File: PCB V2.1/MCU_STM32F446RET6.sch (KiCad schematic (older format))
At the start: 39 parts, among them J1 20021121-00010C4LF, J2 0475890001-MicroUSBPort, P2 CONN_01X03, SW1 B3U-1000P, U1 STM32F446RET6_-_TQFP64, X1 ABM3B8.000MHZB2T, X2 ABS07-32.768KHZ-9-T

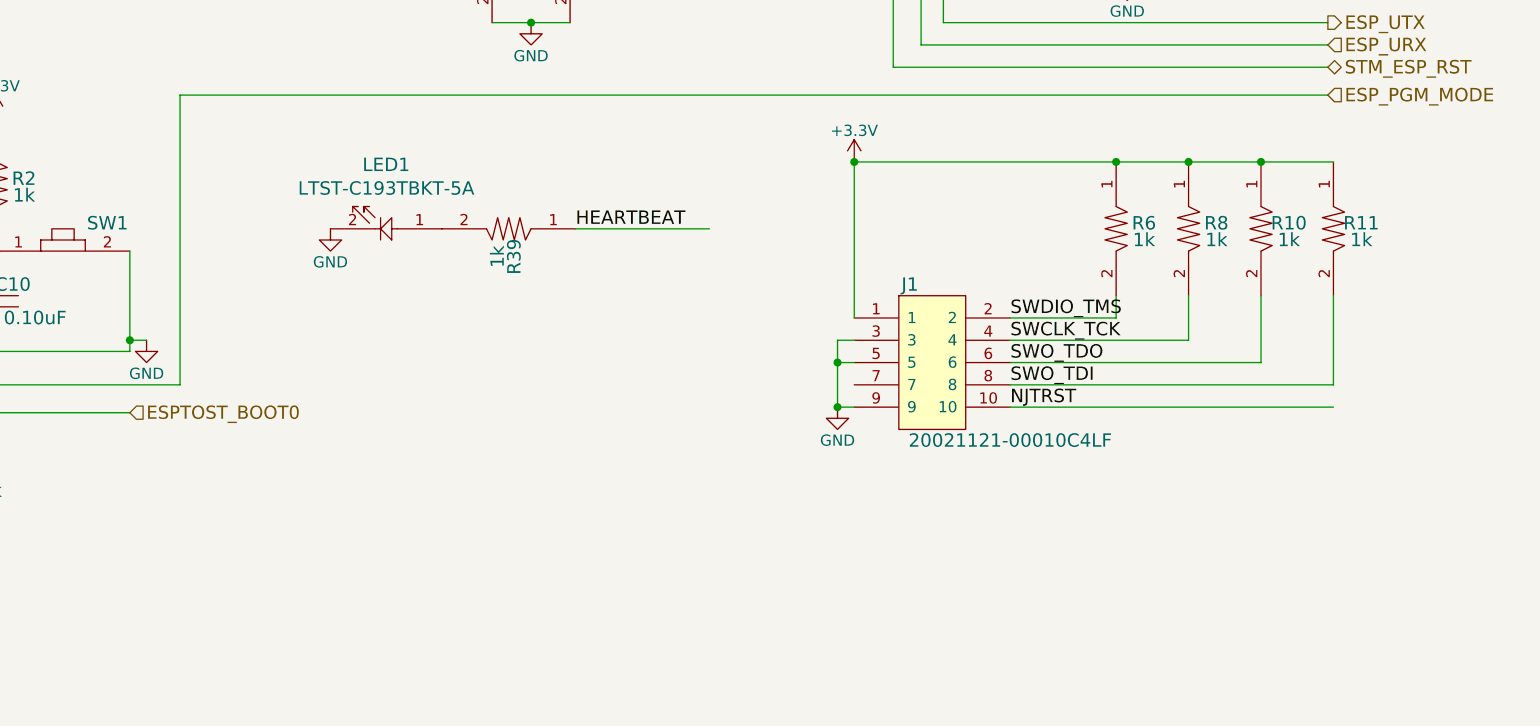
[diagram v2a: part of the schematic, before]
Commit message: DRC clear
all design rule violations cleared.
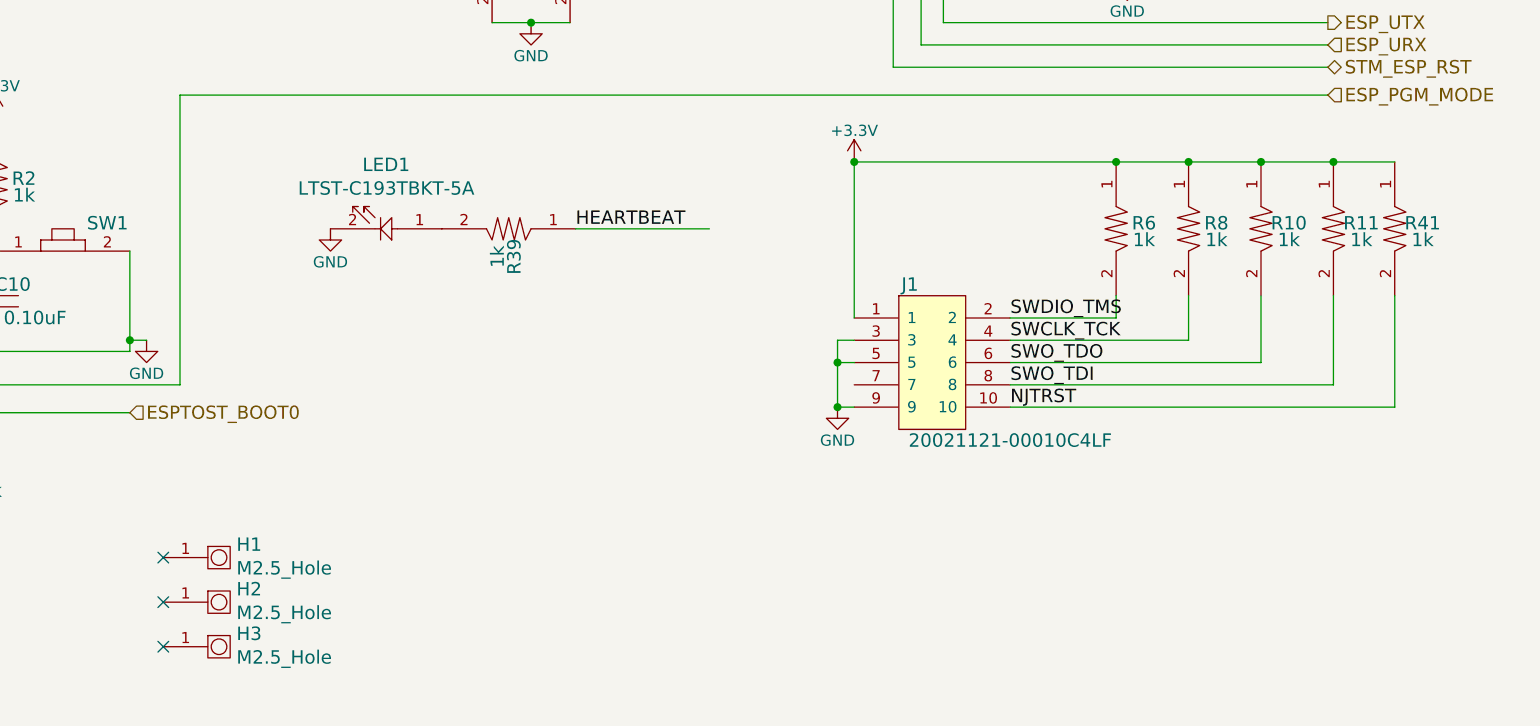
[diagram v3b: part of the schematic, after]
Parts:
- added H1, H2, H3: M2.5_Hole, PCB_Footprints:M2.5_HOLE, symbol M2.5_Hole
- added R41: RC1005F102CS, PCB_Footprints:R0402, symbol RC1005F102CS
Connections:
- wire segments 129 -> 130
- no-connect marks 0 -> 3
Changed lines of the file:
@@
 	10450 6075 10450 5675
 Wire Wire Line
-	9000 6175 10450 6175
-Wire Wire Line
-	8300 5075 10450 5075
+	9000 6175 10725 6175
+Wire Wire Line
+	8300 5075 10725 5075
 Wire Wire Line
 	8300 5075 8300 5775
@@
 	8900 1375 8900 1650
 Connection ~ 8900 1650
+$Comp
+L RC1005F102CS R41
+U 1 1 57E8DE5F
+P 10725 5375
+F 0 "R41" V 10700 5500 60  0000 C CNN
+F 1 "RC1005F102CS" H 10725 5225 60  0001 C CNN
+F 2 "PCB_Footprints:R0402" H 10325 5625 60  0001 C CNN
+F 3 "https://media.digikey.com/pdf/Data%20Sheets/Samsung%20PDFs/RC_Series_ds.pdf" H 10425 5825 60  0001 C CNN
+F 4 "0.00173 @ 5000" H 12275 7325 60  0001 C CNN "Cost"
+F 5 "5 Sept 2016" H 10625 5925 60  0001 C CNN "Date Created"
+F 6 "5 Sept 2016" H 10725 6025 60  0001 C CNN "Date Modified"
+F 7 "Adam Vadala-Roth" H 10825 6125 60  0001 C CNN "Designer"
+F 8 "0.4mm" H 10925 6225 60  0001 C CNN "Height"
+F 9 "Yes" H 11025 6325 60  0001 C CNN "RHoS?"
+F 10 "Samsung Electro-Mechanics America, Inc." H 11125 6425 60  0001 C CNN "MFR"
+F 11 "RC1005F102CS" H 11225 6525 60  0001 C CNN "MFR#"
+F 12 "SMT/SMD" H 11325 6625 60  0001 C CNN "Mounting"
+F 13 "2" H 11425 6725 60  0001 C CNN "Pin Count#"
+F 14 "Active" H 11525 6825 60  0001 C CNN "Status"
+F 15 "%" H 11625 6925 60  0001 C CNN "Tolerance"
+F 16 "passive" H 11725 7025 60  0001 C CNN "Type"
+F 17 "N/A" H 11825 7125 60  0001 C CNN "Voltage"
+F 18 "1/16" H 11925 7225 60  0001 C CNN "Wattage"
+F 19 "1k" V 10775 5500 60  0000 C CNN "Component-Value"
+F 20 "RES SMD 1K OHM 1% 1/16W 0402" H 12125 7425 60  0001 C CNN "Description"
+	1    10725 5375
+	0    1    1    0
+$EndComp
+Connection ~ 10450 5075
+Wire Wire Line
+	10725 6175 10725 5675
+$Comp
+L M2.5_Hole H1
+U 1 1 57E90C74
+P 5450 6850
+F 0 "H1" H 5528 6908 60  0000 L CNN
+F 1 "M2.5_Hole" H 5528 6802 60  0000 L CNN
+F 2 "PCB_Footprints:M2.5_HOLE" H 5075 7300 197 0001 C CNN
+F 3 "" H 5450 6850 197 0001 C CNN
+	1    5450 6850
+	1    0    0    -1
+$EndComp
+$Comp
+L M2.5_Hole H2
+U 1 1 57E90E9E
+P 5450 7050
+F 0 "H2" H 5528 7108 60  0000 L CNN
+F 1 "M2.5_Hole" H 5528 7002 60  0000 L CNN
+F 2 "PCB_Footprints:M2.5_HOLE" H 5075 7500 197 0001 C CNN
+F 3 "" H 5450 7050 197 0001 C CNN
+	1    5450 7050
+	1    0    0    -1
+$EndComp
+$Comp
+L M2.5_Hole H3
+U 1 1 57E90F41
+P 5450 7250
+F 0 "H3" H 5528 7308 60  0000 L CNN
+F 1 "M2.5_Hole" H 5528 7202 60  0000 L CNN
+F 2 "PCB_Footprints:M2.5_HOLE" H 5075 7700 197 0001 C CNN
+F 3 "" H 5450 7250 197 0001 C CNN
+	1    5450 7250
+	1    0    0    -1
+$EndComp
+NoConn ~ 5200 6850
+NoConn ~ 5200 7050
+NoConn ~ 5200 7250
 $EndSCHEMATC

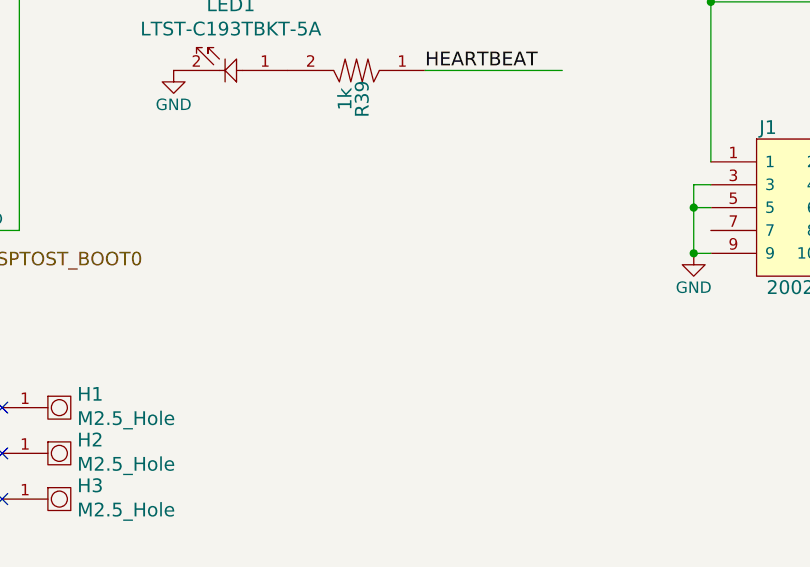
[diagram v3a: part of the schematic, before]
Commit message: 3D and Tweaks
3D files added for components for proper 3D rneder of the board. Board
tweaked, additional ground pours and sticking under neath the ESP-09,
cleaned up routign of JTAG , added labeling of all the pin signals.
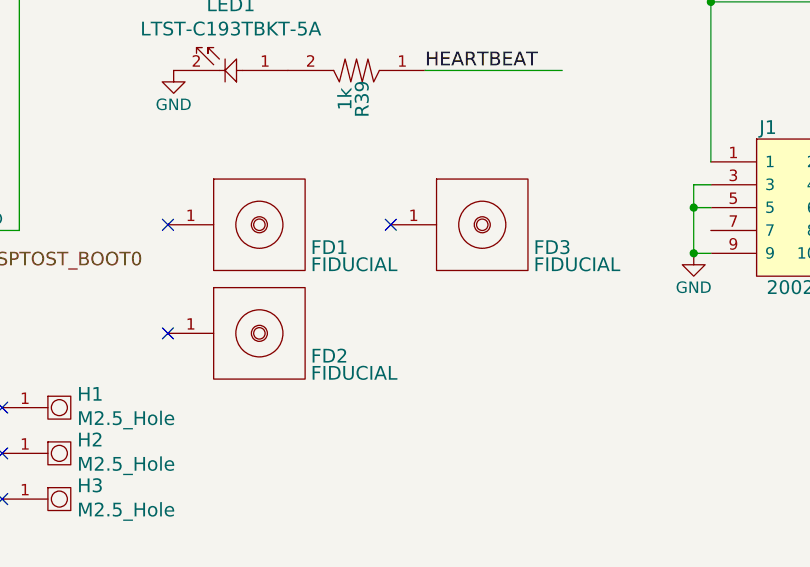
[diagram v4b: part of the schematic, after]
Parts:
- added FD1, FD2, FD3: FIDUCIAL, PCB_Footprints:FIDUCIAL, symbol FIDUCIAL
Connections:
- no-connect marks 3 -> 6
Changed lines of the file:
@@
 NoConn ~ 5200 7050
 NoConn ~ 5200 7250
+$Comp
+L FIDUCIAL FD1
+U 1 1 57ECE3E9
+P 6125 6050
+F 0 "FD1" H 6550 5950 60  0000 L CNN
+F 1 "FIDUCIAL" H 6550 5875 60  0000 L CNN
+F 2 "PCB_Footprints:FIDUCIAL" H 6600 6650 197 0001 C CNN
+F 3 "" H 6125 6050 197 0001 C CNN
+	1    6125 6050
+	1    0    0    -1
+$EndComp
+$Comp
+L FIDUCIAL FD2
+U 1 1 57ECE84C
+P 6125 6525
+F 0 "FD2" H 6550 6425 60  0000 L CNN
+F 1 "FIDUCIAL" H 6550 6350 60  0000 L CNN
+F 2 "PCB_Footprints:FIDUCIAL" H 6600 7125 197 0001 C CNN
+F 3 "" H 6125 6525 197 0001 C CNN
+	1    6125 6525
+	1    0    0    -1
+$EndComp
+$Comp
+L FIDUCIAL FD3
+U 1 1 57ECE916
+P 7100 6050
+F 0 "FD3" H 7525 5950 60  0000 L CNN
+F 1 "FIDUCIAL" H 7525 5875 60  0000 L CNN
+F 2 "PCB_Footprints:FIDUCIAL" H 7575 6650 197 0001 C CNN
+F 3 "" H 7100 6050 197 0001 C CNN
+	1    7100 6050
+	1    0    0    -1
+$EndComp
+NoConn ~ 6900 6050
+NoConn ~ 5925 6050
+NoConn ~ 5925 6525
 $EndSCHEMATC

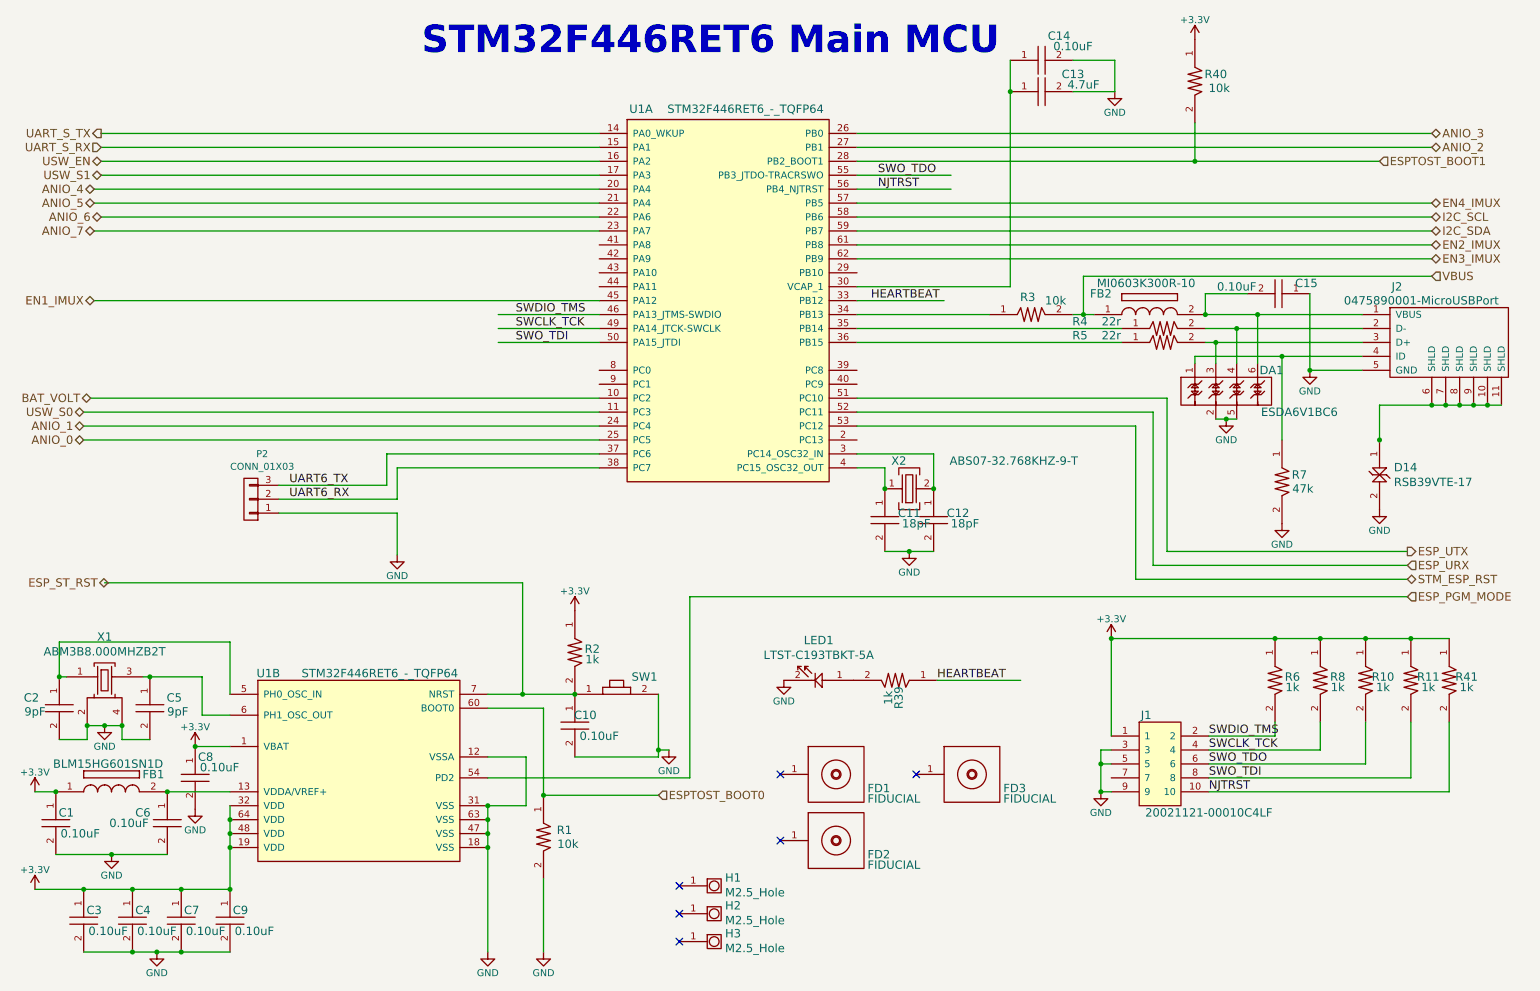
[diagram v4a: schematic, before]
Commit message: Test Points
Test points added as well as some retooling of the PCB overall. More
updates to come before the pending fab
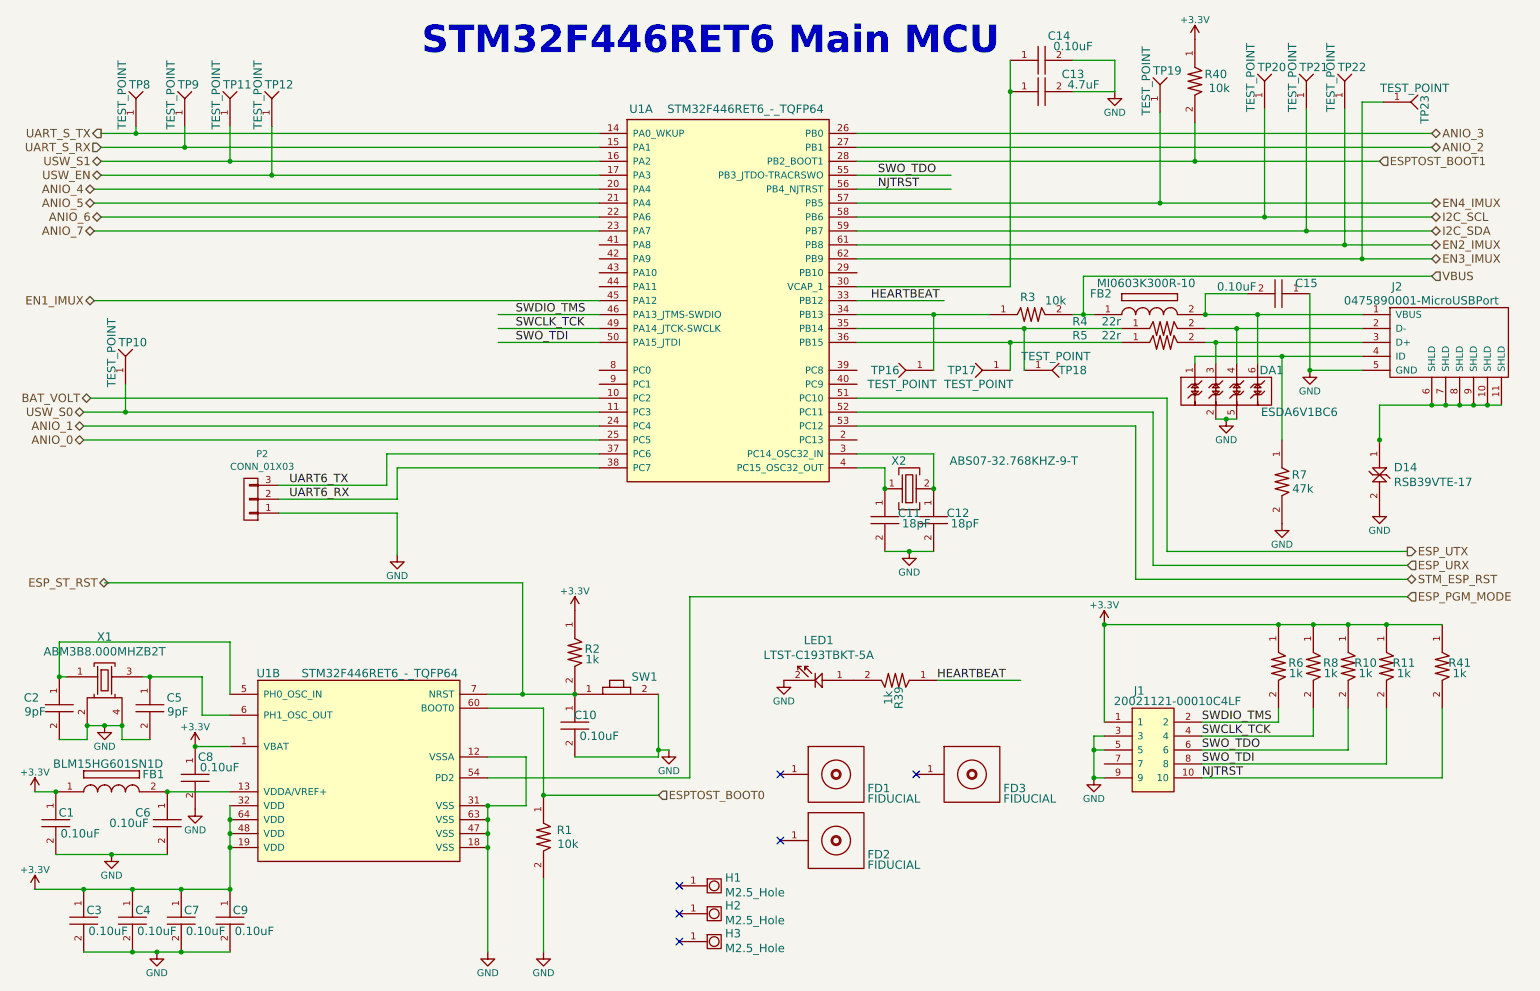
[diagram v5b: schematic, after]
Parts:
- added TP10, TP11, TP12, TP16, TP17, TP18, TP19, TP20, TP21, TP22, TP23, TP8, TP9: TEST_POINT, PCB_Footprints:TEST_POINT, symbol TEST_POINT
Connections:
- wire segments 130 -> 144
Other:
- moved on the sheet: J1, R10, R11, R41, R6, R8

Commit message: JTAG Test Points
Test Points added to JTAG.
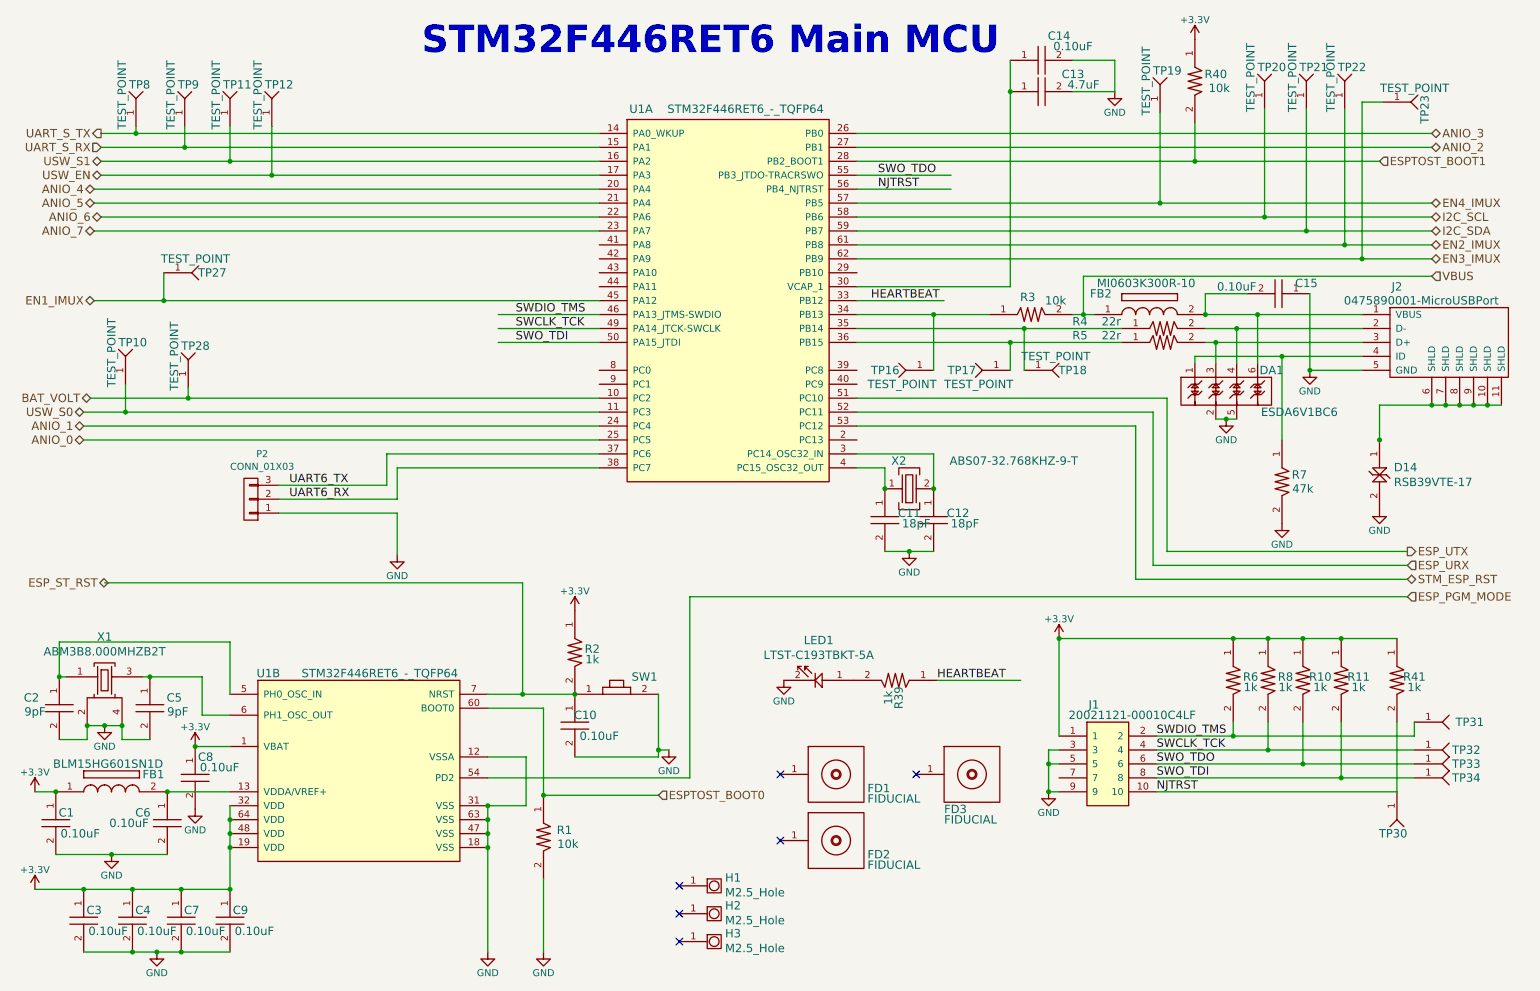
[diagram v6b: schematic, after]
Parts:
- added TP27, TP28, TP30, TP31, TP32, TP33, TP34: TEST_POINT, PCB_Footprints:TEST_POINT, symbol TEST_POINT
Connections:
- wire segments 144 -> 203
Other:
- moved on the sheet: J1, R10, R11, R41, R6, R8
